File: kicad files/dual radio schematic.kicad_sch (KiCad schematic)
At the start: 53 parts, among them J1 Conn_Coaxial, J2 Conn_01x01_Female, J3 Conn_01x01_Female, J4 Conn_01x01_Female, J5 Conn_01x01_Female, J6 Conn_01x01_Female, J7 Conn_01x04_Male, J8 Conn_Coaxial, J9 Conn_01x01_Female, U1 3V3. 500mA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

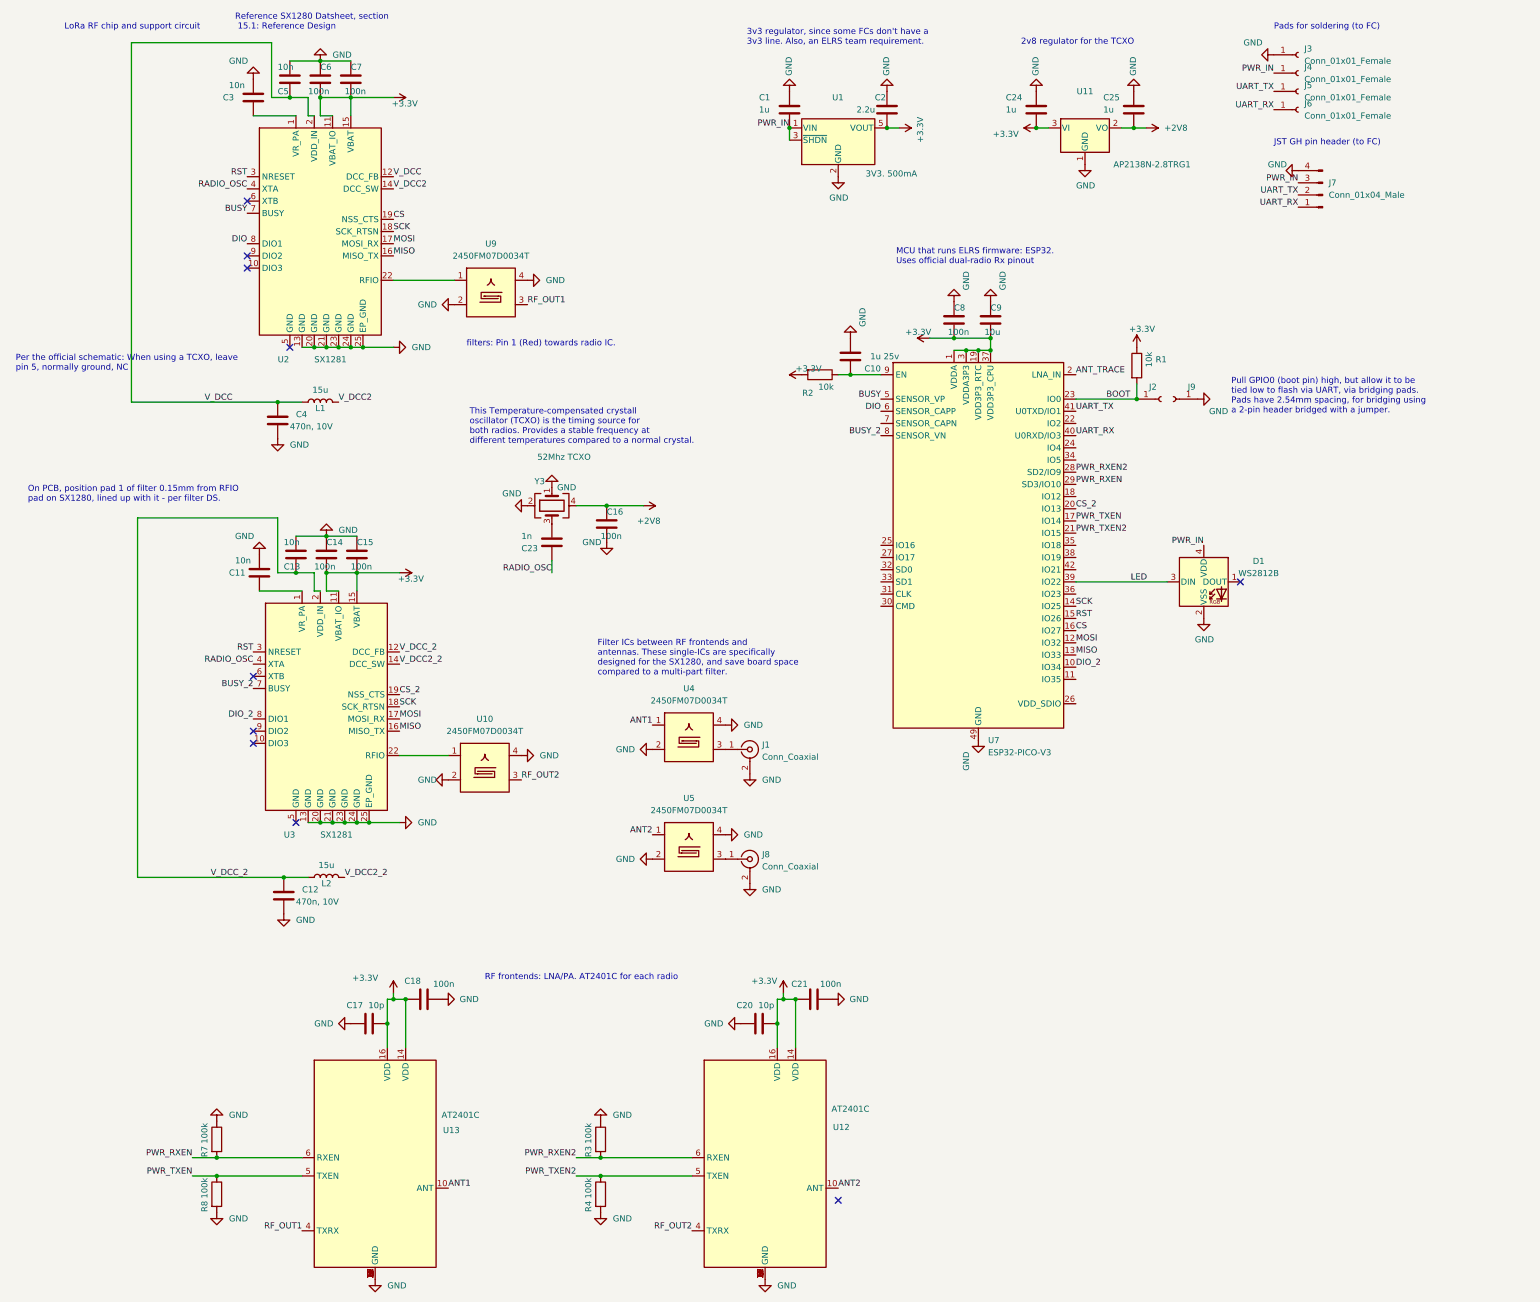
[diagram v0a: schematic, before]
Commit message: Updated dual radio to eliminate second rad's inductor
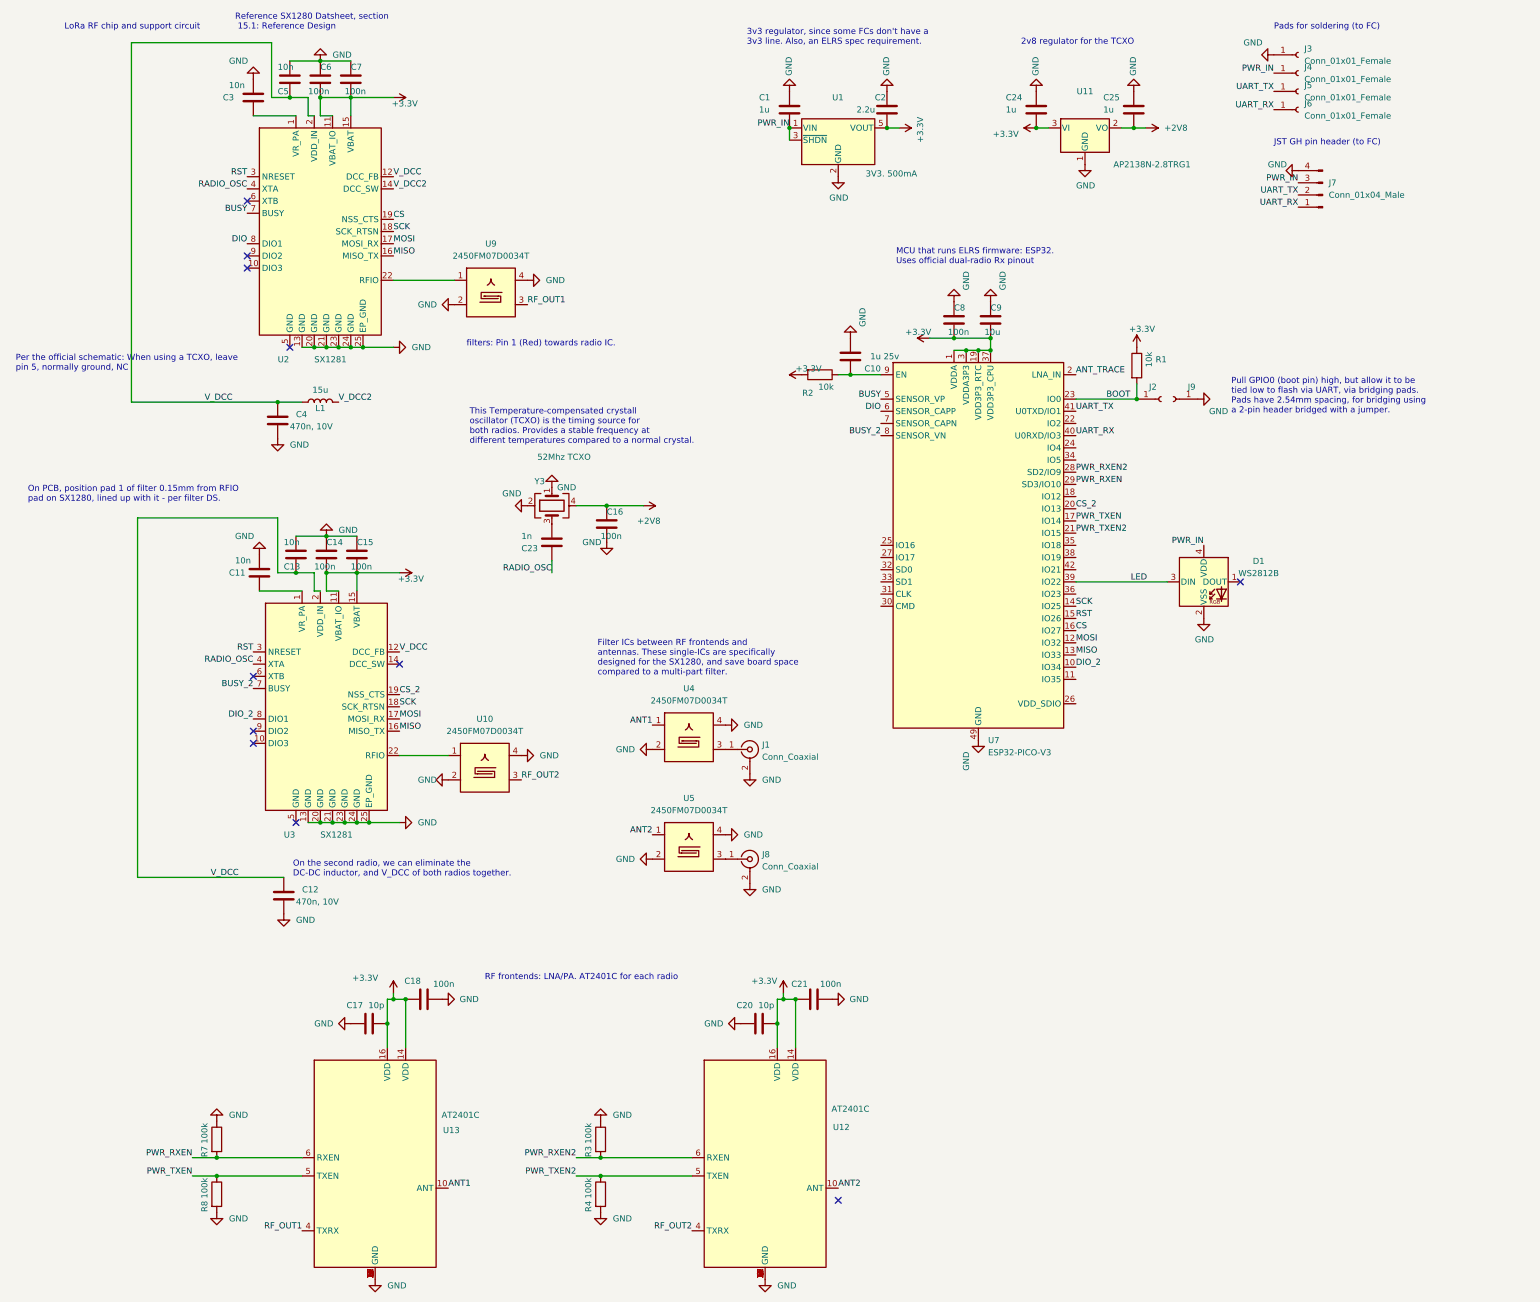
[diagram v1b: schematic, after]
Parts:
- removed L2: 15u, Inductor_SMD:L_0805_2012Metric, symbol Device:L
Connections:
- net V_DCC_2 is gone; now on net V_DCC: C12.1, C13.2, U3.12 (DCC_FB), U3.2 (VDD_IN)
- net V_DCC2_2: no longer names the net of U3.14 (DCC_SW)
- no-connect marks 10 -> 11
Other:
- note added: "3v3 regulator, since some FCs don't have a 3v3 line. Also, an ELRS spec requirement."
- note added: "On the second radio, we can eliminate the DC-DC inductor, and V_DCC of both radios together."
- note removed: "3v3 regulator, since some FCs don't have a 3v3 line. Also, an ELRS team requirement."
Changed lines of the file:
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@@
   (junction (at 173.99 224.79) (diameter 0) (color 0 0 0 0)
-  )
-  (junction (at 71.12 194.31) (diameter 0) (color 0 0 0 0)
   )
   (junction (at 78.74 31.75) (diameter 0) (color 0 0 0 0)
@@
   (no_connect (at 186.69 261.62))
   (no_connect (at 63.5 64.77))
+  (no_connect (at 95.25 149.86))
   (no_connect (at 64.77 163.83))
   (no_connect (at 64.77 152.4))
@@
     (stroke (width 0) (type default) (color 0 0 0 0))
   )
-  (wire (pts (xy 71.12 194.31) (xy 76.2 194.31))
-    (stroke (width 0) (type default) (color 0 0 0 0))
-  )
   (wire (pts (xy 177.8 219.71) (xy 177.8 229.87))
     (stroke (width 0) (type default) (color 0 0 0 0))
@@
     (effects (font (size 1.27 1.27)) (justify left bottom))
   )
-  (text "3v3 regulator, since some FCs don't have a \n3v3 line. Also, an ELRS team requirement."
+  (text "3v3 regulator, since some FCs don't have a \n3v3 line. Also, an ELRS spec requirement."
     (at 167.64 20.955 0)
+    (effects (font (size 1.27 1.27)) (justify left bottom))
+  )
+  (text "On the second radio, we can eliminate the\nDC-DC inductor, and V_DCC of both radios together."
+    (at 73.025 194.31 0)
     (effects (font (size 1.27 1.27)) (justify left bottom))
   )
@@
     (effects (font (size 1.27 1.27)) (justify right bottom))
   )
-  (label "V_DCC2_2" (at 95.25 149.86 0)
-    (effects (font (size 1.27 1.27)) (justify left bottom))
-  )
   (label "CS_2" (at 236.22 117.475 0)
     (effects (font (size 1.27 1.27)) (justify left bottom))
@@
     (effects (font (size 1.27 1.27)) (justify left bottom))
   )
-  (label "V_DCC2_2" (at 83.82 194.31 0)
-    (effects (font (size 1.27 1.27)) (justify left bottom))
-  )
   (label "PWR_IN" (at 277.495 26.67 180)
     (effects (font (size 1.27 1.27)) (justify right bottom))
@@
     (effects (font (size 1.27 1.27)) (justify right bottom))
   )
-  (label "V_DCC_2" (at 95.25 147.32 0)
+  (label "V_DCC" (at 95.25 147.32 0)
     (effects (font (size 1.27 1.27)) (justify left bottom))
   )
@@
     (effects (font (size 1.27 1.27)) (justify left bottom))
   )
-  (label "V_DCC_2" (at 55.88 194.31 0)
+  (label "V_DCC" (at 55.88 194.31 0)
     (effects (font (size 1.27 1.27)) (justify left bottom))
   )
@@
     (pin "1")
   )
-  (symbol (lib_id "Device:L") (at 80.01 194.31 90) (unit 1)
-    (in_bom yes) (on_board yes)
-    (property "Reference" "L2" (id 0) (at 80.01 195.58 90))
-    (property "Value" "15u" (id 1) (at 80.01 191.77 90))
-    (property "Footprint" "Inductor_SMD:L_0805_2012Metric" (id 2) (at 80.01 194.31 0)
-      (effects (font (size 1.27 1.27)) hide)
-    )
-    (property "Datasheet" "~" (id 3) (at 80.01 194.31 0)
-      (effects (font (size 1.27 1.27)) hide)
-    )
-    (property "LCSC" "C486333" (id 4) (at 80.01 194.31 90)
-      (effects (font (size 1.27 1.27)) hide)
-    )
-    (pin "1")
-    (pin "2")
-  )
   (symbol (lib_id "power:GND") (at 166.37 224.79 270) (unit 1)
     (in_bom yes) (on_board yes)
@@
       (reference "L1") (unit 1) (value "15u") (footprint "Inductor_SMD:L_0805_2012Metric")
     )
-    (path "/f8bf492a-5345-44db-872c-d838090462b6"
-      (reference "L2") (unit 1) (value "15u") (footprint "Inductor_SMD:L_0805_2012Metric")
-    )
     (path "/99227391-ce0e-45c3-a5e5-3f921aafe240"

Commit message: Updates including dif filter by antenna, better WiFi PCB antenna, and single inductor
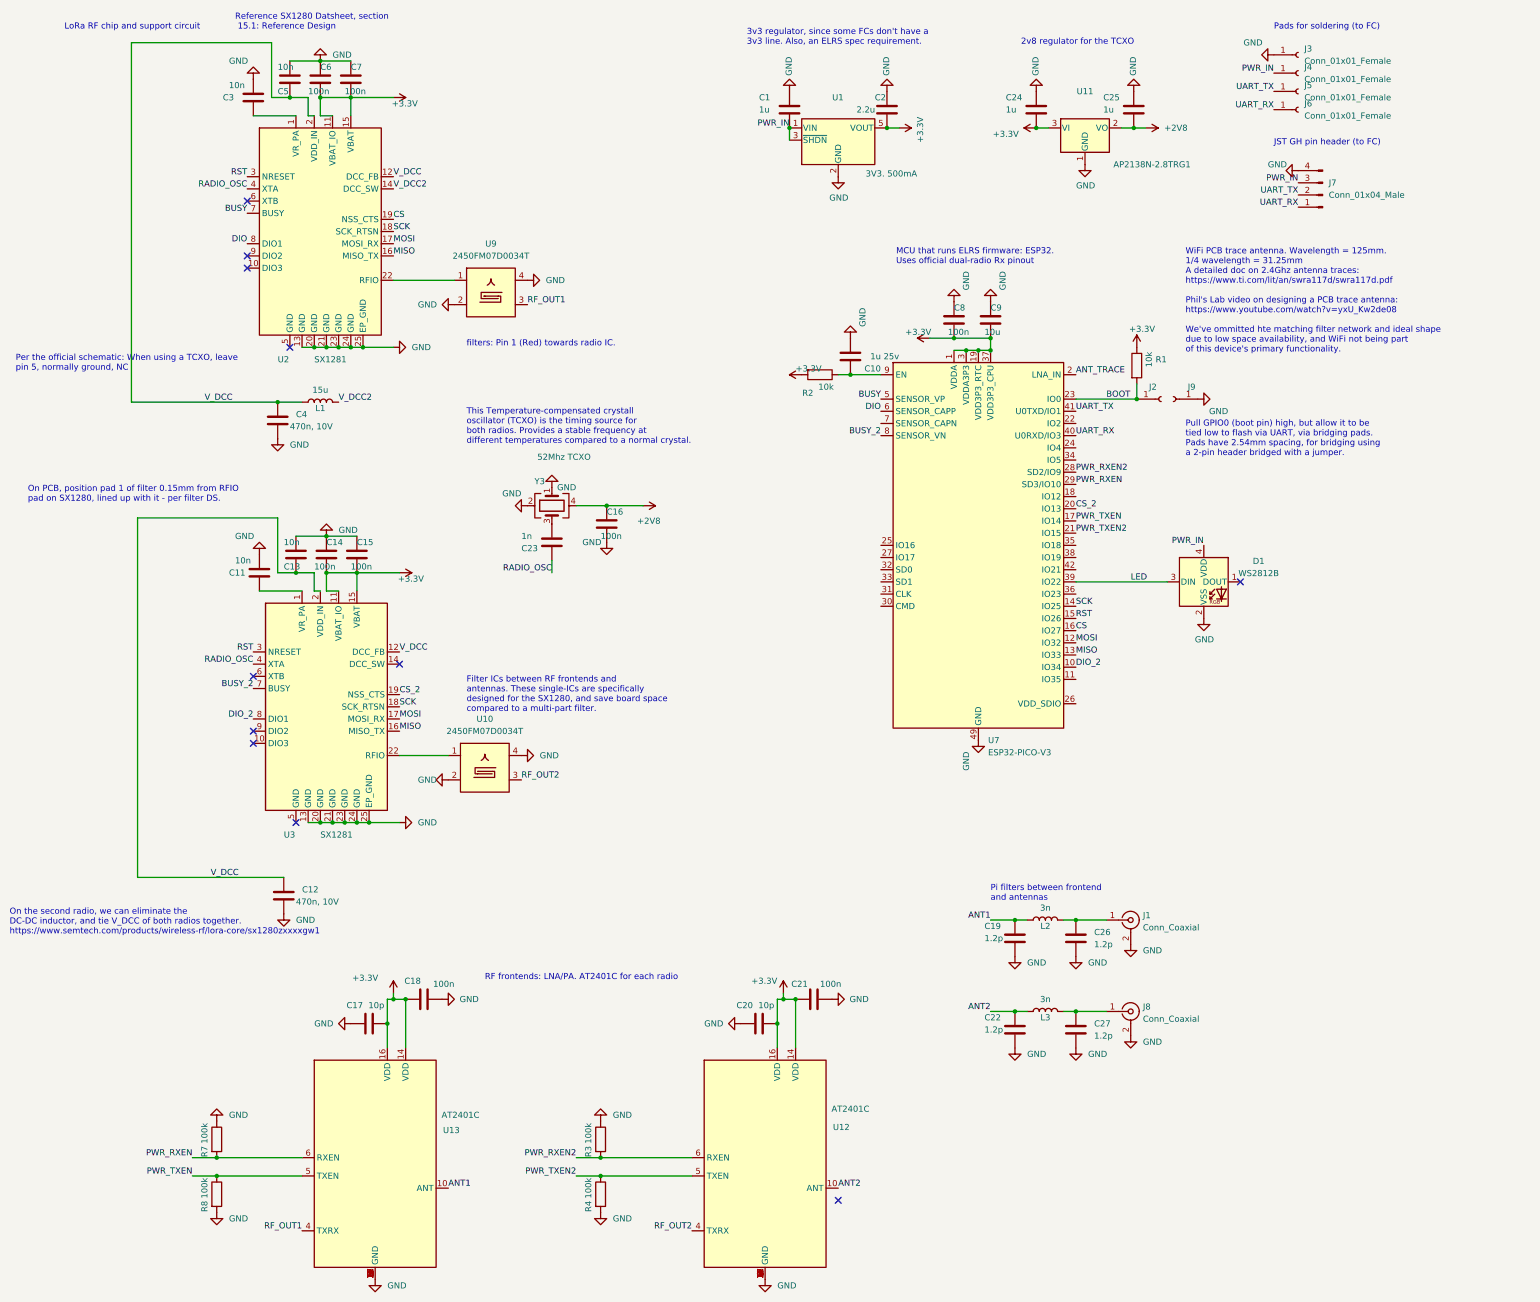
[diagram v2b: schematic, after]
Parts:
- removed U4, U5: 2450FM07D0034T, Anyleaf_Shared:2450FM07D0034, symbol Anyleaf Shared:2450FM07D0034
- added C19, C22, C26, C27: 1.2p, Capacitor_SMD:C_0402_1005Metric, symbol Device:C
- added L2, L3: 3n, Inductor_SMD:L_0402_1005Metric, symbol Device:L
- U2, U3: LCSC C2151551 -> C125969
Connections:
- net ANT1: now also C19.1, L2.1
- net ANT2: now also C22.1, L3.1
- net GND: now also C19.2, C22.2, C26.2, C27.2
- net at J1.1 (In): now also C26.1, L2.2
- net at J8.1 (In): now also C27.1, L3.2
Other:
- note added: "On the second radio, we can eliminate the DC-DC inductor, and tie V_DCC of both radios together. https://www.semtech.com/products/wireless-rf/lora-core/sx1280zxxxxgw1"
- note added: "Pi filters between frontend and antennas"
- note added: "WiFi PCB trace antenna. Wavelength = 125mm. 1/4 wavelength = 31.25mm A detailed doc on 2.4Ghz antenna traces: https://www.ti.com/lit/an/swra117d/swra117d.pdf Phil's Lab video on designing a PCB trace antenna: https://www.youtube.com/watch?v=yxU_Kw2de08 We've ommitted hte matching filter network and ideal shape due to low space availability, and WiFi not being part of this device's primary functio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"
- note removed: "On the second radio, we can eliminate the DC-DC inductor, and V_DCC of both radios together."
- moved on the sheet: J1, J8

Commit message: Updated dual rad to use RFX2401C frontends
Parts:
- removed U12: AT2401C, Package_DFN_QFN:QFN-16-1EP_3x3mm_P0.5mm_EP1.7x1.7mm, symbol Anyleaf Shared:AT2401C
- added U4: RFX2401C, Package_DFN_QFN:QFN-16-1EP_3x3mm_P0.5mm_EP1.7x1.7mm, symbol Anyleaf Shared:AT2401C
- U13: value AT2401C -> RFX2401C; LCSC C783588 -> C19213; LCSC_AT2401C (none) -> C783588
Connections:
- net +3V3: now also U4.14 (VDD), U4.16 (VDD)
- net ANT2: now also U4.10 (ANT)
- net GND: now also U4.1 (GND), U4.11 (GND), U4.12 (GND), U4.15 (GND), U4.17 (GND), U4.2 (GND), U4.3 (GND), U4.7 (GND), U4.8 (GND), U4.9 (GND)
- net PWR_RXEN2: now also U4.6 (RXEN)
- net PWR_TXEN2: now also U4.5 (TXEN)
- net RF_OUT2: now also U4.4 (TXRX)
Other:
- note added: "RF frontends: LNA/PA. RFX2401C for each radio"
- note removed: "RF frontends: LNA/PA. AT2401C for each radio"
